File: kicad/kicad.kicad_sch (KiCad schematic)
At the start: 244 parts, among them sw1 Esc, sw10 Z, sw100 N5, sw101 N6, sw102 N2, sw103 N1, sw104 N0, sw105 MPlay, sw106 MFwd, sw107 NSlash, sw108 NStar, sw109 N8, sw11 LCtrl, sw110 N9, sw111 NMinus, sw112 NPlus, sw113 NEnter, sw114 N3, sw115 NPeriod, sw12 LSys, sw13 F2, sw14 F3, sw15 2, sw16 3, sw17 W, sw18 E, sw19 S, sw2 F1, sw20 D, sw21 X, sw22 C, sw23 LAlt, sw24 THome, sw25 F4, sw26 F5, sw27 4, sw28 5, sw29 R, sw3 Tilda, sw30 T, sw31 F, sw32 G, sw33 V, sw34 B, sw35 LSpace, sw36 TLeft, sw37 F6, sw38 F7, sw39 6, sw4 1, sw40 7, sw41 Y, sw42 U, sw43 H, sw44 J, sw45 N, sw46 M, sw47 TUp, sw48 TDown, sw49 F8, sw5 Tab, sw50 F9, sw51 8, sw52 9, sw53 I, sw54 O, sw55 K, sw56 L, sw57 Comma, sw58 Period, sw59 RSpace, sw6 Q, sw60 TRight, sw61 F10, sw62 F11, sw63 0, sw64 Minus, sw65 P, sw66 LBrack, sw67 Semi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

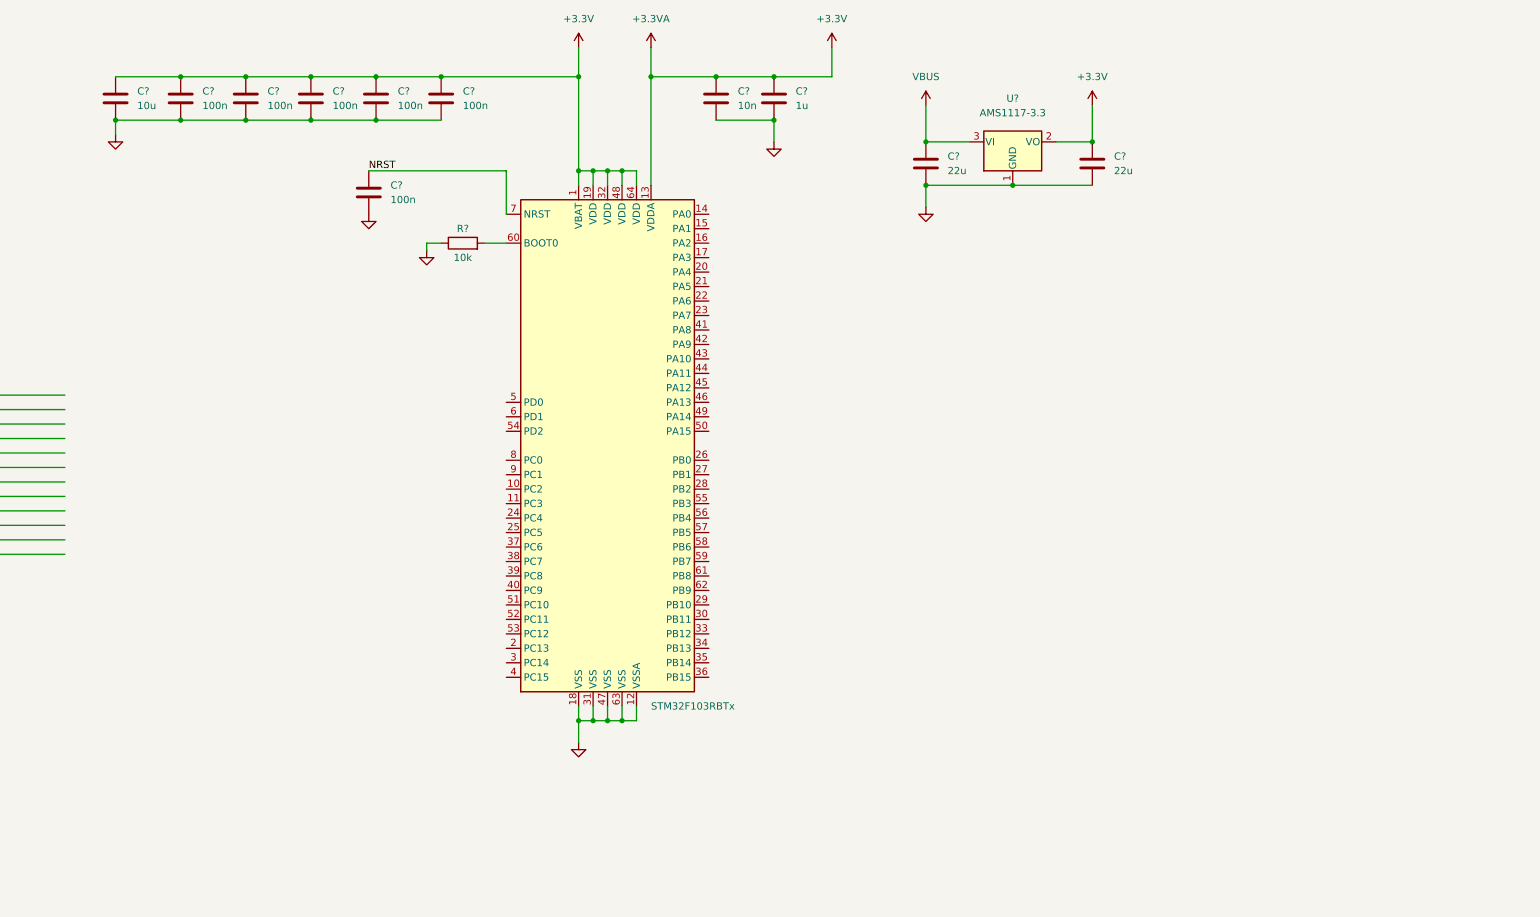
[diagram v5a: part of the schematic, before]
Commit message: Add swd debug, finish usb
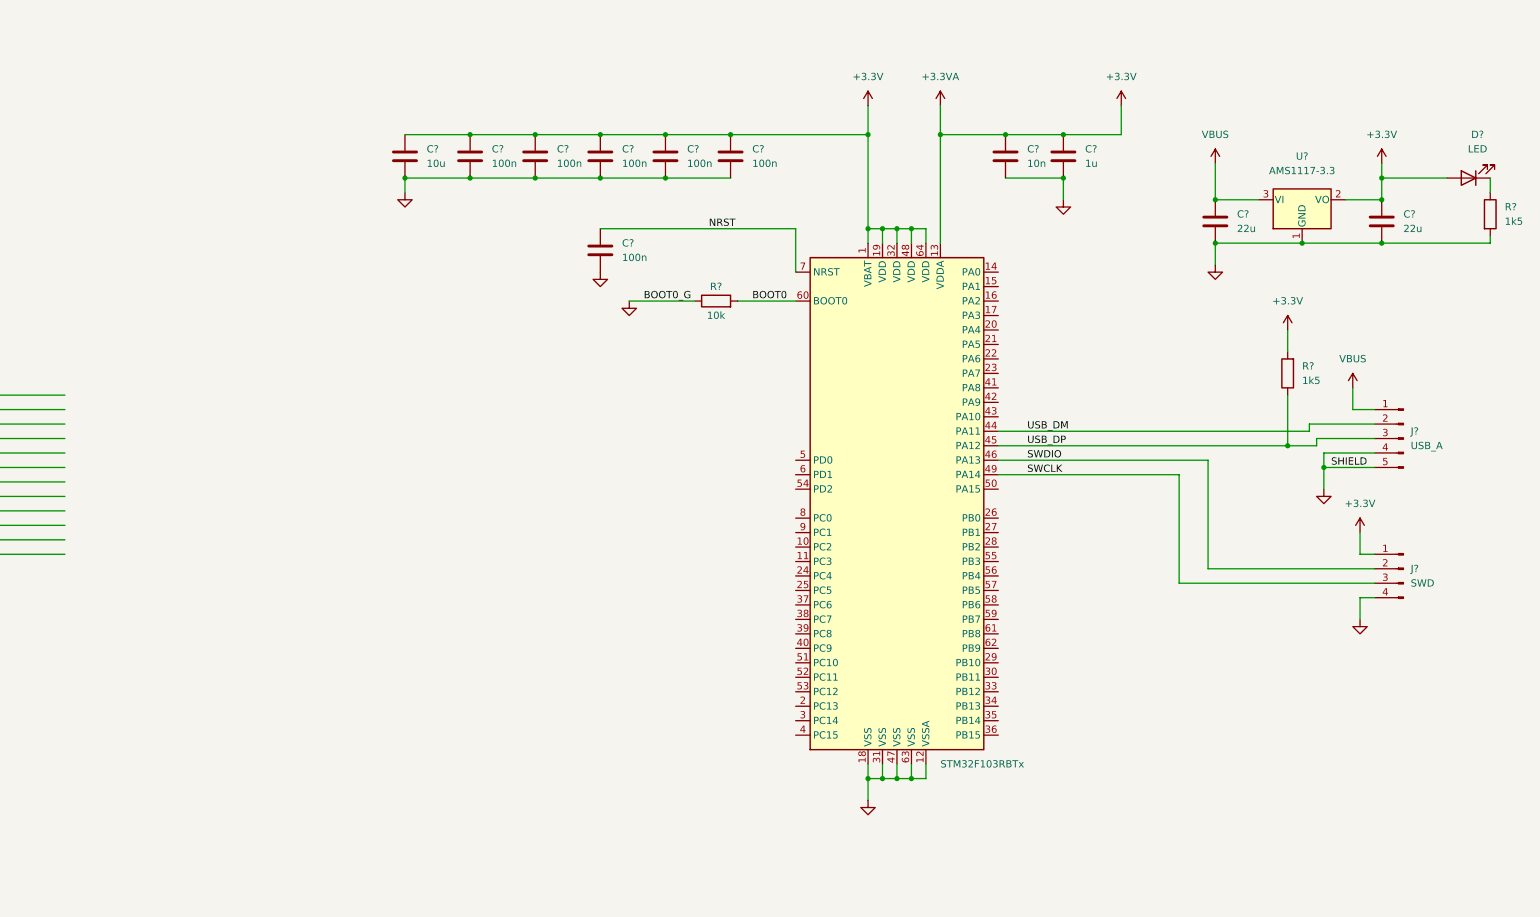
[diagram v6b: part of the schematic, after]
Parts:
- added D?: LED, symbol Device:LED
- added J?: USB_A, symbol Connector:Conn_01x05_Male
- added J?: SWD, symbol Connector:Conn_01x04_Male
- added R? (x2): 1k5, symbol Device:R
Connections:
- net +3.3V: now also D?.2 (A), J?.1 (Pin_1), R?.2
- net GND: now also J?.4 (Pin_4), J?.4 (Pin_4), J?.5 (Pin_5), R?.2
- net VBUS: now also J?.1 (Pin_1)
- net BOOT0: now reaches MCU1.60 (BOOT0), R?.2
- net USB_DM: now reaches MCU1.44 (PA11)
- net USB_DM: now also J?.2 (Pin_2)
- net USB_DP: now reaches MCU1.45 (PA12)
- net USB_DP: now also J?.3 (Pin_3), R?.1
- net SWDIO: now reaches MCU1.46 (PA13)
- net SWDIO: now also J?.2 (Pin_2)
- net SWCLK: now reaches MCU1.49 (PA14)
- net SWCLK: now also J?.3 (Pin_3)
- new net: D?.1 (K), R?.1
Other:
- moved on the sheet: C?, R?, U?

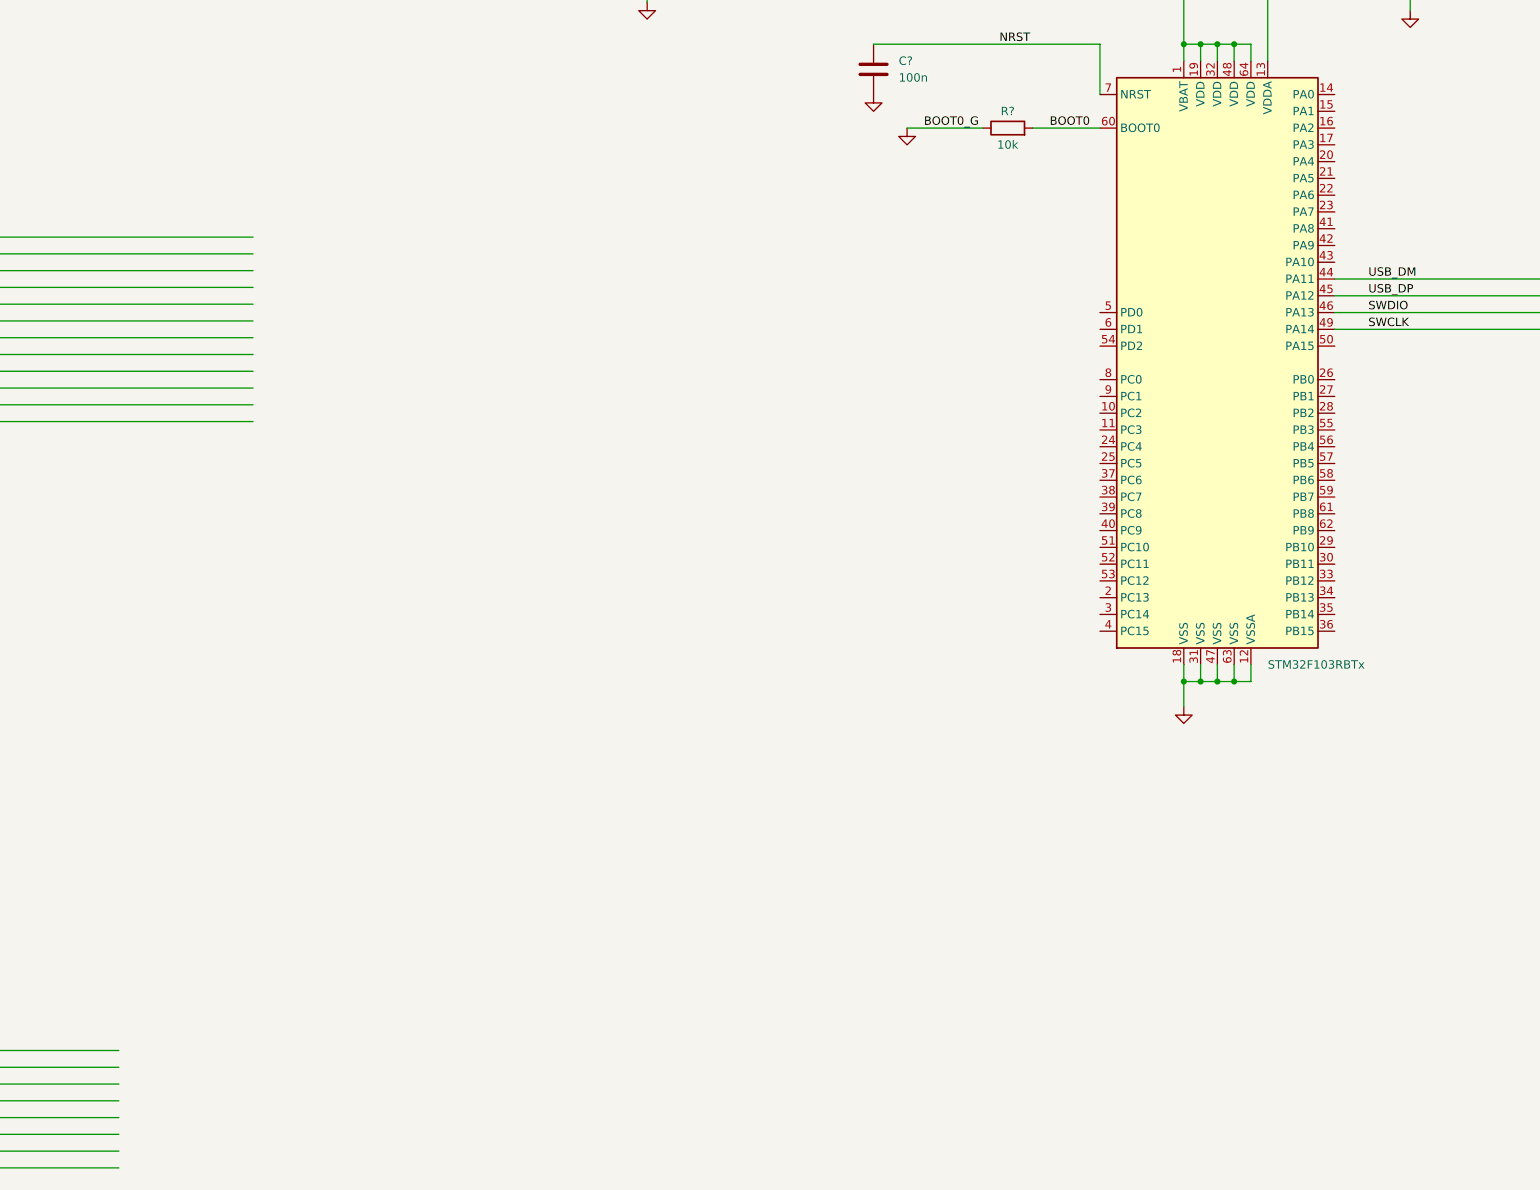
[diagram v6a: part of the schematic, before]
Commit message: Connect matrix to gpio lines
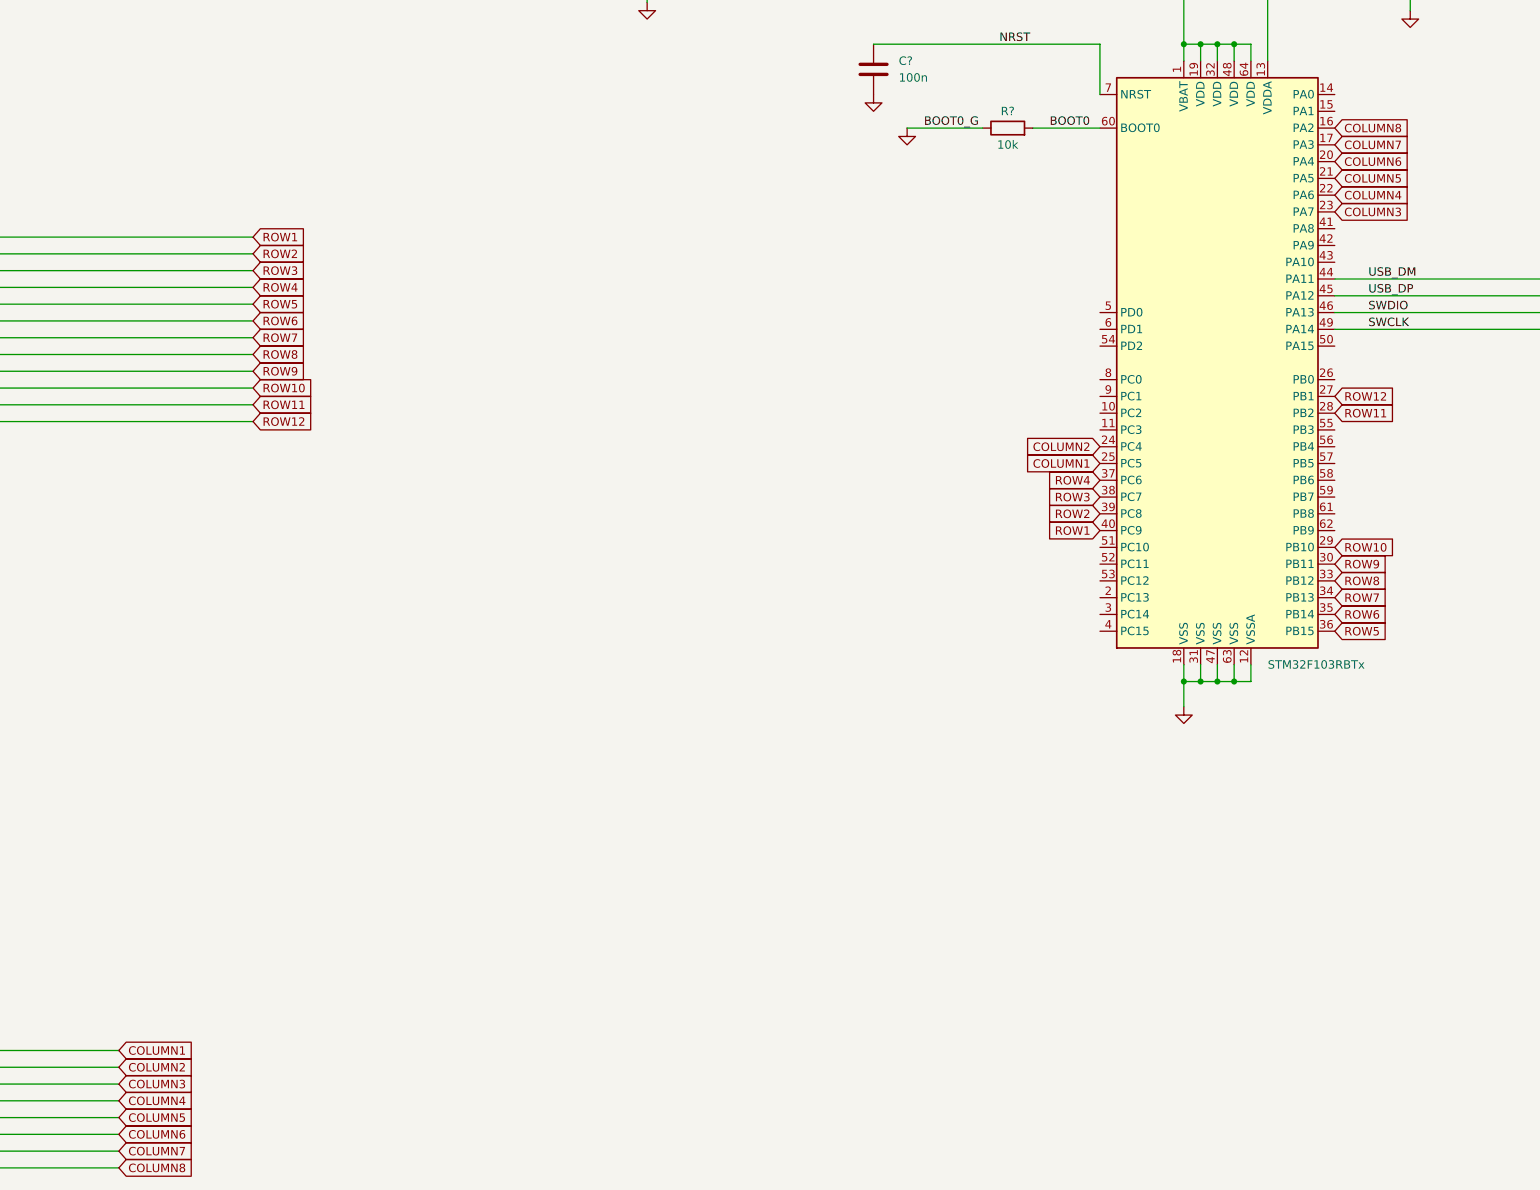
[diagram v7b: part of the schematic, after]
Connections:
- net ROW11: now reaches sw104.1, sw11.1, sw23.1, sw35.1, sw47.1, sw59.1, sw71.1, sw81.1, sw92.1
- net ROW11: now also MCU1.28 (PB2)
- net COLUMN6: now reaches D37.2 (A), D38.2 (A), D39.2 (A), D40.2 (A), D41.2 (A), D42.2 (A), D43.2 (A), D44.2 (A), D45.2 (A), D46.2 (A), D47.2 (A), D48.2 (A)
- net COLUMN6: now also MCU1.20 (PA4)
- net COLUMN5: now reaches D49.2 (A), D50.2 (A), D51.2 (A), D52.2 (A), D53.2 (A), D54.2 (A), D55.2 (A), D56.2 (A), D57.2 (A), D58.2 (A), D59.2 (A), D60.2 (A)
- net COLUMN5: now also MCU1.21 (PA5)
- net COLUMN8: now reaches D1.2 (A), D10.2 (A), D11.2 (A), D2.2 (A), D3.2 (A), D4.2 (A), D5.2 (A), D6.2 (A), D7.2 (A), D8.2 (A), D9.2 (A)
- net COLUMN8: now also MCU1.16 (PA2)
- net ROW7: now reaches sw100.1, sw111.1, sw19.1, sw31.1, sw43.1, sw55.1, sw67.1, sw7.1, sw79.1
- net ROW7: now also MCU1.34 (PB13)
- net ROW1: now reaches sw1.1, sw105.1, sw13.1, sw25.1, sw37.1, sw49.1, sw61.1, sw73.1, sw83.1, sw94.1
- net ROW1: now also MCU1.40 (PC9)
- net ROW10: now reaches sw10.1, sw103.1, sw114.1, sw22.1, sw34.1, sw46.1, sw58.1, sw70.1, sw80.1, sw91.1
- net ROW10: now also MCU1.29 (PB10)
- net ROW12: now reaches sw115.1, sw12.1, sw24.1, sw36.1, sw48.1, sw60.1, sw72.1, sw82.1, sw93.1
- net ROW12: now also MCU1.27 (PB1)
- net ROW6: now reaches sw110.1, sw18.1, sw30.1, sw42.1, sw54.1, sw6.1, sw66.1, sw78.1, sw88.1, sw99.1
- net ROW6: now also MCU1.35 (PB14)
- net COLUMN3: now reaches D73.2 (A), D74.2 (A), D75.2 (A), D76.2 (A), D77.2 (A), D78.2 (A), D79.2 (A), D80.2 (A), D81.2 (A), D82.2 (A)
- net COLUMN3: now also MCU1.23 (PA7)
- net ROW9: now reaches sw102.1, sw113.1, sw21.1, sw33.1, sw45.1, sw57.1, sw69.1, sw9.1, sw90.1
- net ROW9: now also MCU1.30 (PB11)
- net COLUMN4: now reaches D61.2 (A), D62.2 (A), D63.2 (A), D64.2 (A), D65.2 (A), D66.2 (A), D67.2 (A), D68.2 (A), D69.2 (A), D70.2 (A), D71.2 (A), D72.2 (A)
- net COLUMN4: now also MCU1.22 (PA6)
- net COLUMN1: now reaches D105.2 (A), D106.2 (A), D107.2 (A), D108.2 (A), D109.2 (A), D110.2 (A), D111.2 (A), D112.2 (A), D113.2 (A), D114.2 (A), D115.2 (A)
- net COLUMN1: now also MCU1.25 (PC5)
- net ROW3: now reaches sw107.1, sw15.1, sw27.1, sw3.1, sw39.1, sw51.1, sw63.1, sw75.1, sw85.1, sw96.1
- net ROW3: now also MCU1.38 (PC7)
- net ROW4: now reaches sw108.1, sw16.1, sw28.1, sw4.1, sw40.1, sw52.1, sw64.1, sw76.1, sw86.1, sw97.1
- net ROW4: now also MCU1.37 (PC6)
- net COLUMN7: now reaches D25.2 (A), D26.2 (A), D27.2 (A), D28.2 (A), D29.2 (A), D30.2 (A), D31.2 (A), D32.2 (A), D33.2 (A), D34.2 (A), D35.2 (A), D36.2 (A)
- net COLUMN7: now also MCU1.17 (PA3)
- net ROW2: now reaches sw106.1, sw14.1, sw2.1, sw26.1, sw38.1, sw50.1, sw62.1, sw74.1, sw84.1, sw95.1
- net ROW2: now also MCU1.39 (PC8)
- net COLUMN2: now reaches D83.2 (A), D84.2 (A), D85.2 (A), D86.2 (A), D87.2 (A), D88.2 (A), D89.2 (A), D91.2 (A), D92.2 (A), D93.2 (A)
- net COLUMN2: now also MCU1.24 (PC4)
- net ROW5: now reaches sw109.1, sw17.1, sw29.1, sw41.1, sw5.1, sw53.1, sw65.1, sw77.1, sw87.1, sw98.1
- net ROW5: now also MCU1.36 (PB15)
- net ROW8: now reaches sw101.1, sw112.1, sw20.1, sw32.1, sw44.1, sw56.1, sw68.1, sw8.1, sw89.1
- net ROW8: now also MCU1.33 (PB12)
